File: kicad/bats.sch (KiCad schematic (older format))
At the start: 28 parts, among them P1 SERVO, SW1 RESET, SW2 SHOT, SW3 UP, SW4 LEFT, SW5 DOWN, SW6 RIGHT, U1 BUZZER

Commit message: Casi rematado
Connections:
- net ARD0: now also R12.1, SW5.2; no longer R13.1, SW6.2
- net ARD1: now also R13.1, SW6.2; no longer R12.1, SW5.2
- net ARD2: now also R9.1, SW2.2; no longer R10.1, SW3.2
- net ARD3: now also R10.1, SW3.2; no longer R9.1, SW2.2
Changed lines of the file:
@@
 	10500 4650 8950 4650
 Text Label 8950 4650 2    60   ~ 0
-ARD0
+ARD1
 Connection ~ 10200 4700
 Wire Wire Line
 	10200 4700 8700 4700
 Text Label 8700 4700 2    60   ~ 0
-ARD1
+ARD0
 Connection ~ 9900 4750
 Wire Wire Line
@@
 	9600 4800 8200 4800
 Text Label 8200 4800 2    60   ~ 0
-ARD2
+ARD3
 Connection ~ 9300 4850
 Wire Wire Line
 	9300 4850 7950 4850
 Text Label 7950 4850 2    60   ~ 0
-ARD3
+ARD2
 $Comp
 L SW_PUSHBUTTON SW3

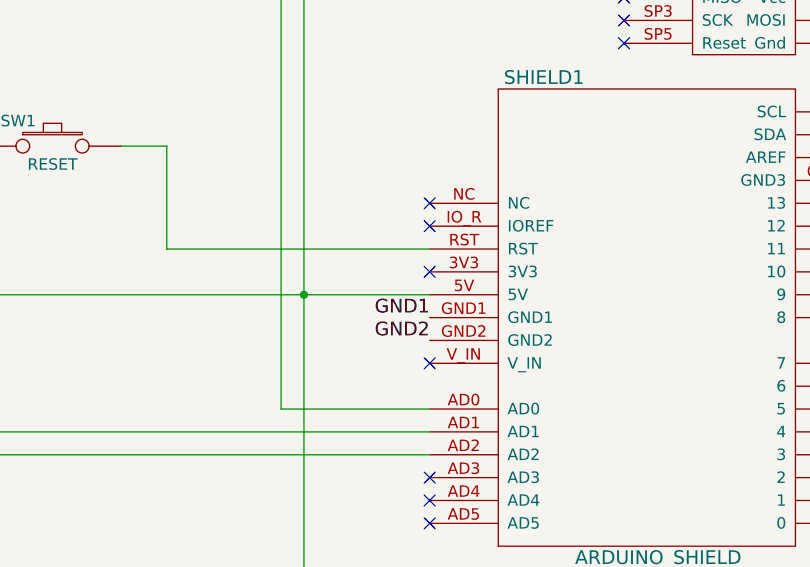
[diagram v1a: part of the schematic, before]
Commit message: Engadida area de recheo no fronte da placa
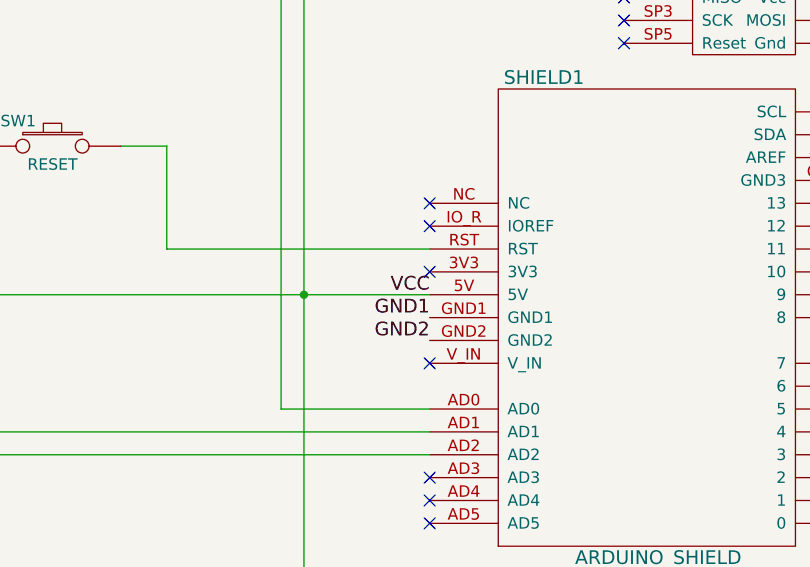
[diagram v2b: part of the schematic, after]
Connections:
- net VCC: now reaches P1.1 (P1), R1.1, SHIELD1.5V, SW2.1, SW3.1, SW4.1, SW5.1, SW6.1, VR1.1, VR2.1
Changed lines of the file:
@@
 	0    1    1    0
 $EndComp
+Text Label 4850 3850 2    60   ~ 0
+VCC
 $EndSCHEMATC

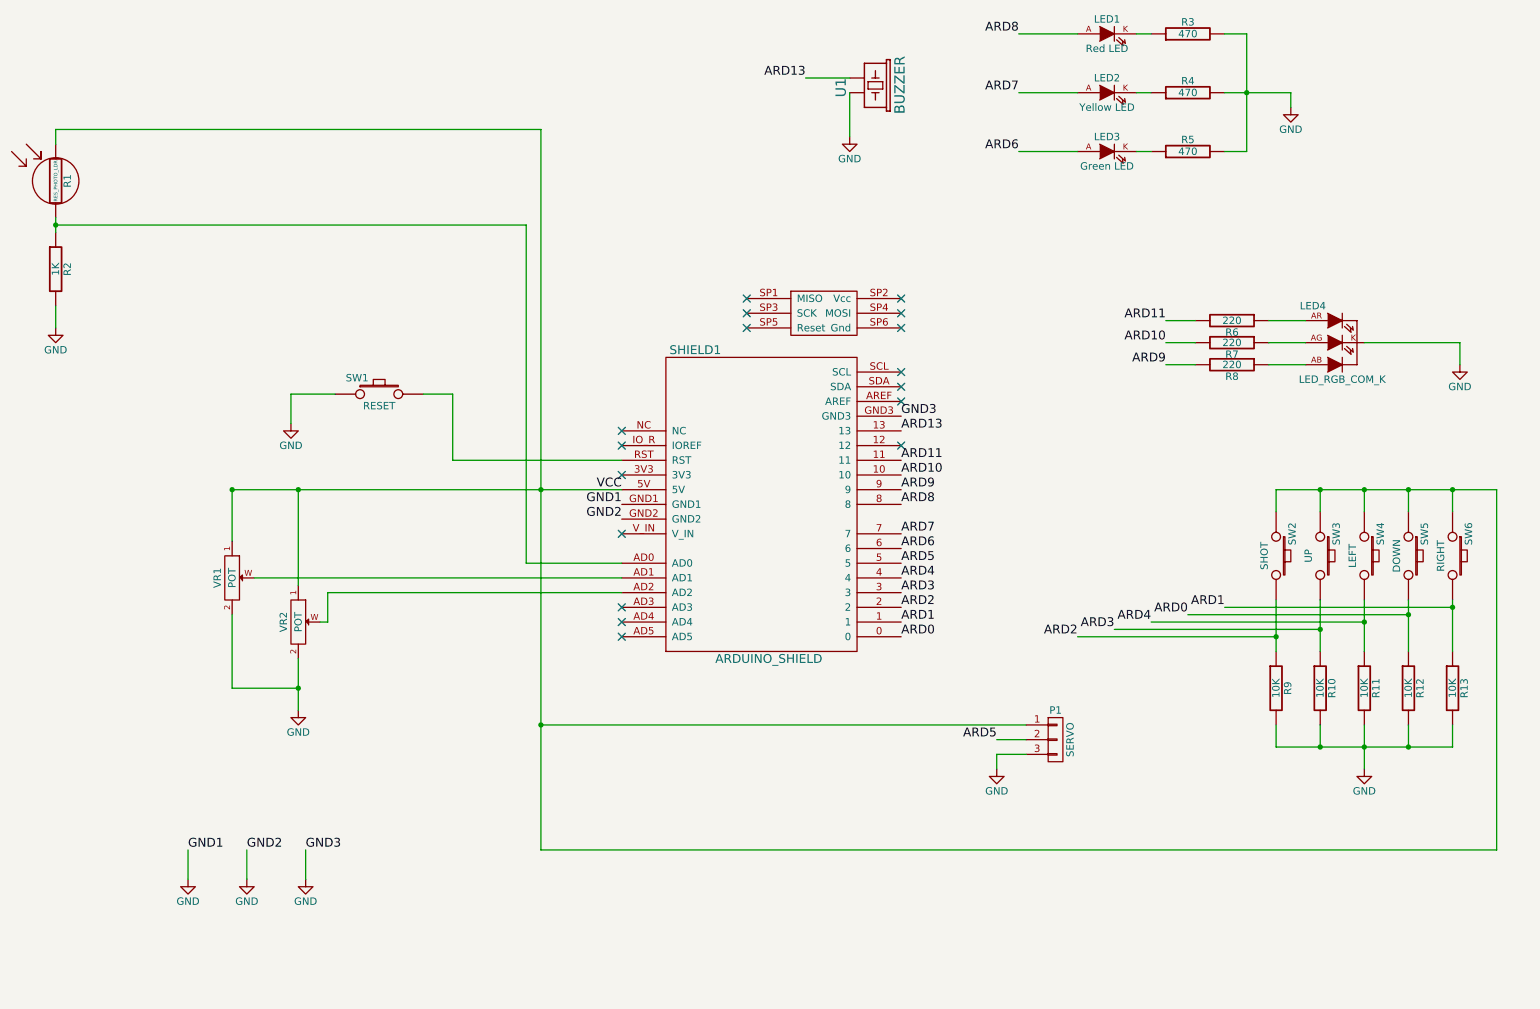
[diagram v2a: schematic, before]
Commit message: Cambios masivos:
Issue 01 - Cambiados os botóns de D0 e D1 a AD4 e AD5 respectivamente.
Issue 02 - Cambiada a posición dos dous potes e do led rgb cara ao
interior da placa.
Issue 05 - Serigrafiados os pines de control
Issue 06 - Sustituido o buzzer

Además simplifícase todo o enrutado da placa.
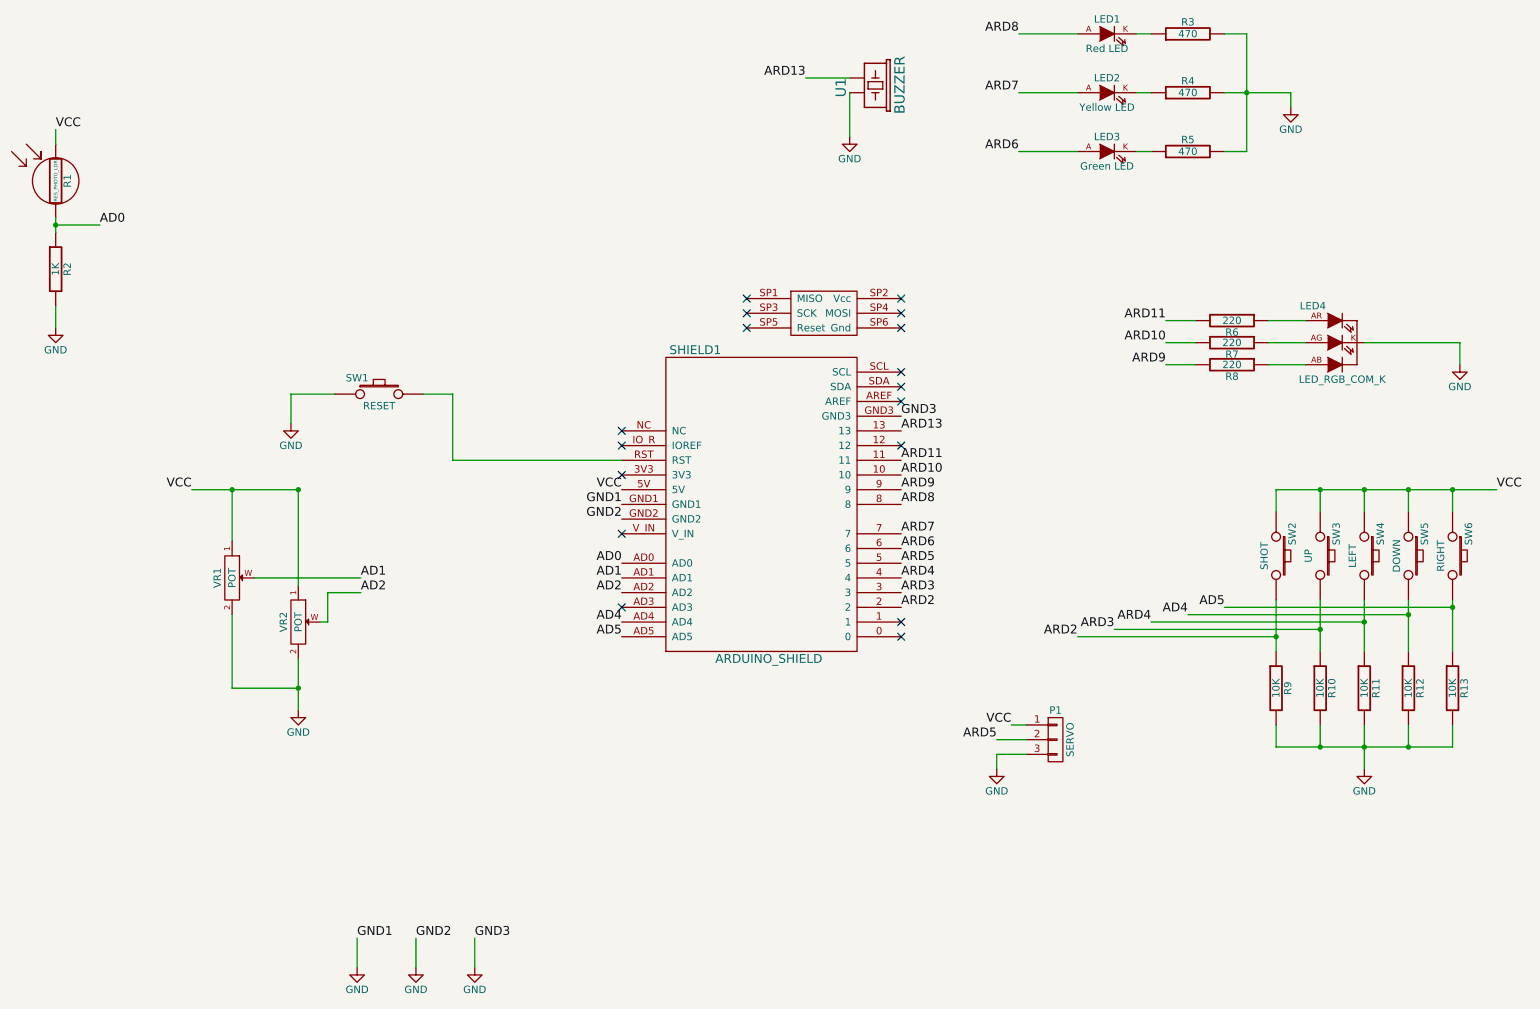
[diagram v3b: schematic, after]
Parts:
- U1: footprint Buzzers_Beepers:MagneticBuzzer_Kingstate_KCG0601 -> Buzzers_Beepers:Buzzer_12x9.5RM7.6
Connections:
- net AD0: now reaches R1.2, R2.1, SHIELD1.AD0
- net AD1: now reaches SHIELD1.AD1, VR1.W
- net AD2: now reaches SHIELD1.AD2, VR2.W
- net AD4: now reaches SHIELD1.AD4
- net AD4: now also R12.1, SW5.2
- net AD5: now reaches SHIELD1.AD5
- net AD5: now also R13.1, SW6.2
- removed net ARD0: R12.1, SHIELD1.0, SW5.2
- removed net ARD1: R13.1, SHIELD1.1, SW6.2
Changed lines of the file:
@@
 Sheet 1 1
 Title "BATS: BricoLabs Arduino Training Shield"
-Date "2015-06-23"
-Rev "0.0"
+Date "2016-01-05"
+Rev "2.0"
 Comp "BricoLabs"
 Comment1 ""
@@
 F 0 "U1" H 6500 850 70  0000 L BNN
 F 1 "BUZZER" H 6350 1250 70  0000 L BNN
-F 2 "Buzzers_Beepers:MagneticBuzzer_Kingstate_KCG0601" H 6500 1050 60  0001 C CNN
+F 2 "Buzzers_Beepers:Buzzer_12x9.5RM7.6" H 6500 1050 60  0001 C CNN
 F 3 "" H 6500 1050 60  0000 C CNN
 	1    6550 1100
@@
 	1    0    0    -1
 $EndComp
-NoConn ~ 4850 4750
-NoConn ~ 4850 4850
 NoConn ~ 4850 3450
 NoConn ~ 4850 3550
@@
 L GND #PWR09
 U 1 1 558C28FA
-P 1900 6500
-F 0 "#PWR09" H 1900 6250 50  0001 C CNN
-F 1 "GND" H 1900 6350 50  0000 C CNN
-F 2 "" H 1900 6500 60  0000 C CNN
-F 3 "" H 1900 6500 60  0000 C CNN
-	1    1900 6500
-	1    0    0    -1
-$EndComp
-Text Label 1900 6300 0    60   ~ 0
+P 3050 7100
+F 0 "#PWR09" H 3050 6850 50  0001 C CNN
+F 1 "GND" H 3050 6950 50  0000 C CNN
+F 2 "" H 3050 7100 60  0000 C CNN
+F 3 "" H 3050 7100 60  0000 C CNN
+	1    3050 7100
+	1    0    0    -1
+$EndComp
+Text Label 3050 6900 0    60   ~ 0
 GND1
 Text Label 4850 4050 2    60   ~ 0
@@
 L GND #PWR010
 U 1 1 558C3402
-P 2300 6500
-F 0 "#PWR010" H 2300 6250 50  0001 C CNN
-F 1 "GND" H 2300 6350 50  0000 C CNN
-F 2 "" H 2300 6500 60  0000 C CNN
-F 3 "" H 2300 6500 60  0000 C CNN
-	1    2300 6500
-	1    0    0    -1
-$EndComp
-Text Label 2300 6300 0    60   ~ 0
+P 3450 7100
+F 0 "#PWR010" H 3450 6850 50  0001 C CNN
+F 1 "GND" H 3450 6950 50  0000 C CNN
+F 2 "" H 3450 7100 60  0000 C CNN
+F 3 "" H 3450 7100 60  0000 C CNN
+	1    3450 7100
+	1    0    0    -1
+$EndComp
+Text Label 3450 6900 0    60   ~ 0
 GND2
 $Comp
 L GND #PWR011
 U 1 1 558C5111
-P 2700 6500
-F 0 "#PWR011" H 2700 6250 50  0001 C CNN
-F 1 "GND" H 2700 6350 50  0000 C CNN
-F 2 "" H 2700 6500 60  0000 C CNN
-F 3 "" H 2700 6500 60  0000 C CNN
-	1    2700 6500
-	1    0    0    -1
-$EndComp
-Text Label 2700 6300 0    60   ~ 0
+P 3850 7100
+F 0 "#PWR011" H 3850 6850 50  0001 C CNN
+F 1 "GND" H 3850 6950 50  0000 C CNN
+F 2 "" H 3850 7100 60  0000 C CNN
+F 3 "" H 3850 7100 60  0000 C CNN
+	1    3850 7100
+	1    0    0    -1
+$EndComp
+Text Label 3850 6900 0    60   ~ 0
 GND3
 Text Label 6750 3350 0    60   ~ 0
@@
 Wire Wire Line
 	1000 2600 1000 2750
-Wire Wire Line
-	4850 4350 4200 4350
-Wire Wire Line
-	4200 4350 4200 2050
-Wire Wire Line
-	4200 2050 1000 2050
 Connection ~ 1000 2050
-Wire Wire Line
-	4300 1400 4300 6300
-Wire Wire Line
-	4300 1400 1000 1400
 Wire Wire Line
 	1000 1400 1000 1500
@@
 Wire Wire Line
 	7400 5650 7400 5750
-Connection ~ 4300 3850
-Wire Wire Line
-	4300 5450 7600 5450
-Wire Wire Line
-	10800 3850 10800 6300
-Wire Wire Line
-	10800 6300 4300 6300
-Connection ~ 4300 5450
 Connection ~ 2200 3850
 Connection ~ 2650 3850
@@
 	2600 3200 2600 3400
 Wire Wire Line
-	1900 6300 1900 6500
-Wire Wire Line
-	2300 6500 2300 6300
+	3050 6900 3050 7100
+Wire Wire Line
+	3450 7100 3450 6900
 Wire Wire Line
 	2200 3850 2200 4200
@@
 	2650 3850 2650 4500
 Wire Wire Line
-	4850 4450 2350 4450
-Wire Wire Line
-	4850 4550 2850 4550
-Wire Wire Line
 	2850 4550 2850 4750
 Wire Wire Line
 	2850 4750 2800 4750
 Wire Wire Line
-	2700 6500 2700 6300
-Wire Wire Line
-	2200 3850 4850 3850
+	3850 7100 3850 6900
 $Comp
 L POT VR1
@@
 	9300 5450 9300 5600
 Connection ~ 9600 5600
-Text Label 6750 4850 0    60   ~ 0
-ARD0
-Text Label 6750 4750 0    60   ~ 0
-ARD1
 Text Label 6750 4650 0    60   ~ 0
 ARD2
@@
 	10500 4650 8950 4650
 Text Label 8950 4650 2    60   ~ 0
-ARD1
+AD5
 Connection ~ 10200 4700
 Wire Wire Line
 	10200 4700 8700 4700
 Text Label 8700 4700 2    60   ~ 0
-ARD0
+AD4
 Connection ~ 9900 4750
 Wire Wire Line
@@
 Text Label 4850 3850 2    60   ~ 0
 VCC
+NoConn ~ 6750 4750
+NoConn ~ 6750 4850
+Text Label 4850 4750 2    60   ~ 0
+AD4
+Text Label 4850 4850 2    60   ~ 0
+AD5
+Wire Wire Line
+	1925 3850 2650 3850
+Text Label 1925 3850 2    60   ~ 0
+VCC
+Text Label 1000 1400 0    60   ~ 0
+VCC
+Wire Wire Line
+	7600 5450 7500 5450
+Text Label 7500 5450 2    60   ~ 0
+VCC
+Text Label 10800 3850 0    60   ~ 0
+VCC
+Wire Wire Line
+	1000 2050 1300 2050
+Text Label 1300 2050 0    60   ~ 0
+AD0
+Text Label 4850 4350 2    60   ~ 0
+AD0
+Wire Wire Line
+	2350 4450 3075 4450
+Wire Wire Line
+	2850 4550 3075 4550
+Text Label 3075 4450 0    60   ~ 0
+AD1
+Text Label 3075 4550 0    60   ~ 0
+AD2
+Text Label 4850 4450 2    60   ~ 0
+AD1
+Text Label 4850 4550 2    60   ~ 0
+AD2
 $EndSCHEMATC

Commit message: Engadimos algunha serigrafía mais. Todo semella estar listo para a segunda versión.
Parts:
- R2: value 1K -> 10K
- R3, R4, R5: value 470 -> 220
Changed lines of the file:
@@
 P 8700 1550
 F 0 "R5" V 8780 1550 50  0000 C CNN
-F 1 "470" V 8700 1550 50  0000 C CNN
+F 1 "220" V 8700 1550 50  0000 C CNN
 F 2 "Resistors_ThroughHole:Resistor_Horizontal_RM10mm" H 8700 1550 60  0001 C CNN
 F 3 "" H 8700 1550 60  0000 C CNN
@@
 P 8700 1150
 F 0 "R4" V 8780 1150 50  0000 C CNN
-F 1 "470" V 8700 1150 50  0000 C CNN
+F 1 "220" V 8700 1150 50  0000 C CNN
 F 2 "Resistors_ThroughHole:Resistor_Horizontal_RM10mm" H 8700 1150 60  0001 C CNN
 F 3 "" H 8700 1150 60  0000 C CNN
@@
 P 8700 750
 F 0 "R3" V 8780 750 50  0000 C CNN
-F 1 "470" V 8700 750 50  0000 C CNN
+F 1 "220" V 8700 750 50  0000 C CNN
 F 2 "Resistors_ThroughHole:Resistor_Horizontal_RM10mm" H 8700 750 60  0001 C CNN
 F 3 "" H 8700 750 60  0000 C CNN
@@
 P 1000 2350
 F 0 "R2" V 1080 2350 50  0000 C CNN
-F 1 "1K" V 1000 2350 50  0000 C CNN
+F 1 "10K" V 1000 2350 50  0000 C CNN
 F 2 "Resistors_ThroughHole:Resistor_Horizontal_RM10mm" H 1000 2350 60  0001 C CNN
 F 3 "" H 1000 2350 60  0000 C CNN

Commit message: Cambiadas as pegadas das resistencias a furados mais pequenos.
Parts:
- R1, R10, R11, R12, R13, R2, R3, R4, R5, R6, R7, R8, R9: footprint Resistors_ThroughHole:Resistor_Horizontal_RM10mm -> extra:Resistor_Horizontal_SmallHole_RM10mm
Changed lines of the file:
@@
 F 0 "R5" V 8780 1550 50  0000 C CNN
 F 1 "220" V 8700 1550 50  0000 C CNN
-F 2 "Resistors_ThroughHole:Resistor_Horizontal_RM10mm" H 8700 1550 60  0001 C CNN
+F 2 "extra:Resistor_Horizontal_SmallHole_RM10mm" H 8700 1550 60  0001 C CNN
 F 3 "" H 8700 1550 60  0000 C CNN
 	1    8700 1550
@@
 F 0 "R4" V 8780 1150 50  0000 C CNN
 F 1 "220" V 8700 1150 50  0000 C CNN
-F 2 "Resistors_ThroughHole:Resistor_Horizontal_RM10mm" H 8700 1150 60  0001 C CNN
+F 2 "extra:Resistor_Horizontal_SmallHole_RM10mm" H 8700 1150 60  0001 C CNN
 F 3 "" H 8700 1150 60  0000 C CNN
 	1    8700 1150
@@
 F 0 "R3" V 8780 750 50  0000 C CNN
 F 1 "220" V 8700 750 50  0000 C CNN
-F 2 "Resistors_ThroughHole:Resistor_Horizontal_RM10mm" H 8700 750 60  0001 C CNN
+F 2 "extra:Resistor_Horizontal_SmallHole_RM10mm" H 8700 750 60  0001 C CNN
 F 3 "" H 8700 750 60  0000 C CNN
 	1    8700 750
@@
 F 0 "R1" V 1080 1750 50  0000 C CNN
 F 1 "RES_PHOTO_LDR" V 1000 1750 24  0000 C CNN
-F 2 "Resistors_ThroughHole:Resistor_Horizontal_RM10mm" H 1000 1750 60  0001 C CNN
+F 2 "extra:Resistor_Horizontal_SmallHole_RM10mm" H 1000 1750 60  0001 C CNN
 F 3 "" H 1000 1750 60  0000 C CNN
 	1    1000 1750
@@
 F 0 "R2" V 1080 2350 50  0000 C CNN
 F 1 "10K" V 1000 2350 50  0000 C CNN
-F 2 "Resistors_ThroughHole:Resistor_Horizontal_RM10mm" H 1000 2350 60  0001 C CNN
+F 2 "extra:Resistor_Horizontal_SmallHole_RM10mm" H 1000 2350 60  0001 C CNN
 F 3 "" H 1000 2350 60  0000 C CNN
 	1    1000 2350
@@
 F 0 "R10" V 9680 5200 50  0000 C CNN
 F 1 "10K" V 9600 5200 50  0000 C CNN
-F 2 "Resistors_ThroughHole:Resistor_Horizontal_RM10mm" H 9600 5200 60  0001 C CNN
+F 2 "extra:Resistor_Horizontal_SmallHole_RM10mm" H 9600 5200 60  0001 C CNN
 F 3 "" H 9600 5200 60  0000 C CNN
 	1    9600 5200
@@
 F 0 "R11" V 9980 5200 50  0000 C CNN
 F 1 "10K" V 9900 5200 50  0000 C CNN
-F 2 "Resistors_ThroughHole:Resistor_Horizontal_RM10mm" H 9900 5200 60  0001 C CNN
+F 2 "extra:Resistor_Horizontal_SmallHole_RM10mm" H 9900 5200 60  0001 C CNN
 F 3 "" H 9900 5200 60  0000 C CNN
 	1    9900 5200
@@
 F 0 "R12" V 10280 5200 50  0000 C CNN
 F 1 "10K" V 10200 5200 50  0000 C CNN
-F 2 "Resistors_ThroughHole:Resistor_Horizontal_RM10mm" H 10200 5200 60  0001 C CNN
+F 2 "extra:Resistor_Horizontal_SmallHole_RM10mm" H 10200 5200 60  0001 C CNN
 F 3 "" H 10200 5200 60  0000 C CNN
 	1    10200 5200
@@
 F 0 "R13" V 10580 5200 50  0000 C CNN
 F 1 "10K" V 10500 5200 50  0000 C CNN
-F 2 "Resistors_ThroughHole:Resistor_Horizontal_RM10mm" H 10500 5200 60  0001 C CNN
+F 2 "extra:Resistor_Horizontal_SmallHole_RM10mm" H 10500 5200 60  0001 C CNN
 F 3 "" H 10500 5200 60  0000 C CNN
 	1    10500 5200
@@
 F 0 "R6" V 9080 2700 50  0000 C CNN
 F 1 "220" V 9000 2700 50  0000 C CNN
-F 2 "Resistors_ThroughHole:Resistor_Horizontal_RM10mm" H 9000 2700 60  0001 C CNN
+F 2 "extra:Resistor_Horizontal_SmallHole_RM10mm" H 9000 2700 60  0001 C CNN
 F 3 "" H 9000 2700 60  0000 C CNN
 	1    9000 2700
@@
 F 0 "R7" V 9080 2850 50  0000 C CNN
 F 1 "220" V 9000 2850 50  0000 C CNN
-F 2 "Resistors_ThroughHole:Resistor_Horizontal_RM10mm" H 9000 2850 60  0001 C CNN
+F 2 "extra:Resistor_Horizontal_SmallHole_RM10mm" H 9000 2850 60  0001 C CNN
 F 3 "" H 9000 2850 60  0000 C CNN
 	1    9000 2850
@@
 F 0 "R8" V 9080 3000 50  0000 C CNN
 F 1 "220" V 9000 3000 50  0000 C CNN
-F 2 "Resistors_ThroughHole:Resistor_Horizontal_RM10mm" H 9000 3000 60  0001 C CNN
+F 2 "extra:Resistor_Horizontal_SmallHole_RM10mm" H 9000 3000 60  0001 C CNN
 F 3 "" H 9000 3000 60  0000 C CNN
 	1    9000 3000
@@
 F 0 "R9" V 9380 5200 50  0000 C CNN
 F 1 "10K" V 9300 5200 50  0000 C CNN
-F 2 "Resistors_ThroughHole:Resistor_Horizontal_RM10mm" H 9300 5200 60  0001 C CNN
+F 2 "extra:Resistor_Horizontal_SmallHole_RM10mm" H 9300 5200 60  0001 C CNN
 F 3 "" H 9300 5200 60  0000 C CNN
 	1    9300 5200

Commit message: Cambiados os LED a LED de 5mm no esquema e mais no ficheiro net
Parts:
- LED1, LED2, LED3: footprint FT:LED-3MM -> FT:LED-5MM
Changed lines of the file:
@@
 F 0 "LED3" H 8150 1650 50  0000 C CNN
 F 1 "Green LED" H 8150 1450 50  0000 C CNN
-F 2 "FT:LED-3MM" H 8150 1550 60  0001 C CNN
+F 2 "FT:LED-5MM" H 8150 1550 60  0001 C CNN
 F 3 "" H 8150 1550 60  0000 C CNN
 	1    8150 1550
@@
 F 0 "LED2" H 8150 1250 50  0000 C CNN
 F 1 "Yellow LED" H 8150 1050 50  0000 C CNN
-F 2 "FT:LED-3MM" H 8150 1150 60  0001 C CNN
+F 2 "FT:LED-5MM" H 8150 1150 60  0001 C CNN
 F 3 "" H 8150 1150 60  0000 C CNN
 	1    8150 1150
@@
 F 0 "LED1" H 8150 850 50  0000 C CNN
 F 1 "Red LED" H 8150 650 50  0000 C CNN
-F 2 "FT:LED-3MM" H 8150 750 60  0001 C CNN
+F 2 "FT:LED-5MM" H 8150 750 60  0001 C CNN
 F 3 "" H 8150 750 60  0000 C CNN
 	1    8150 750
